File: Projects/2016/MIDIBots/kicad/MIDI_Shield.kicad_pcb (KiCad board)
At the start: 2 copper layers, 92.7 x 82.5 mm, 71 parts, among them IC1 PC900V, K1 SRVO1, K2 SRVO2, K3 SRVO3, P10 A3, P11 A4, P12 AUX_12V, P13 AUX_12V, P14 AUX_5V, P15 AUX_5V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

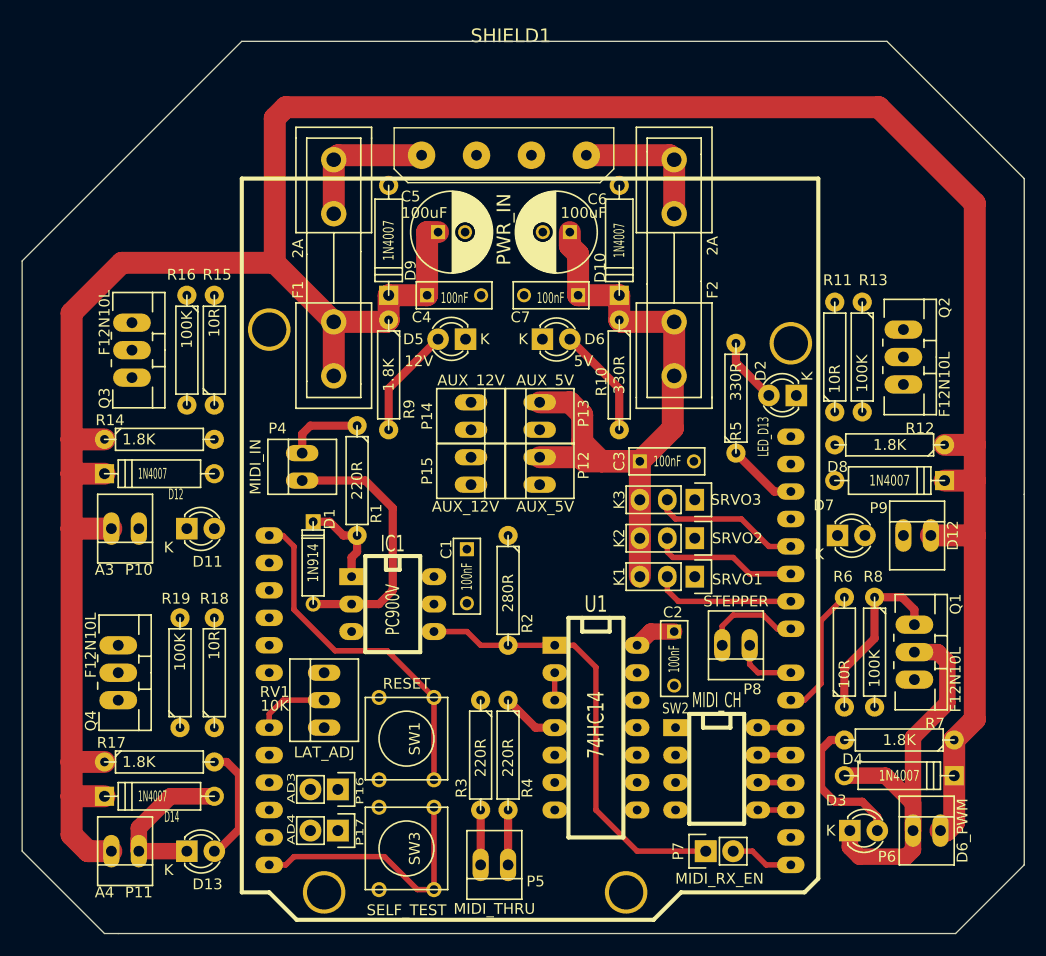
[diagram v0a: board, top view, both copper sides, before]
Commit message: [Y] Flip resistors around MOSFET circuits and reroute tracks [Y] Add 12V aux track [Y] Route VCC tracks/zones [Y] Fixed some unconnected track segments [Y] Moved some reference labels
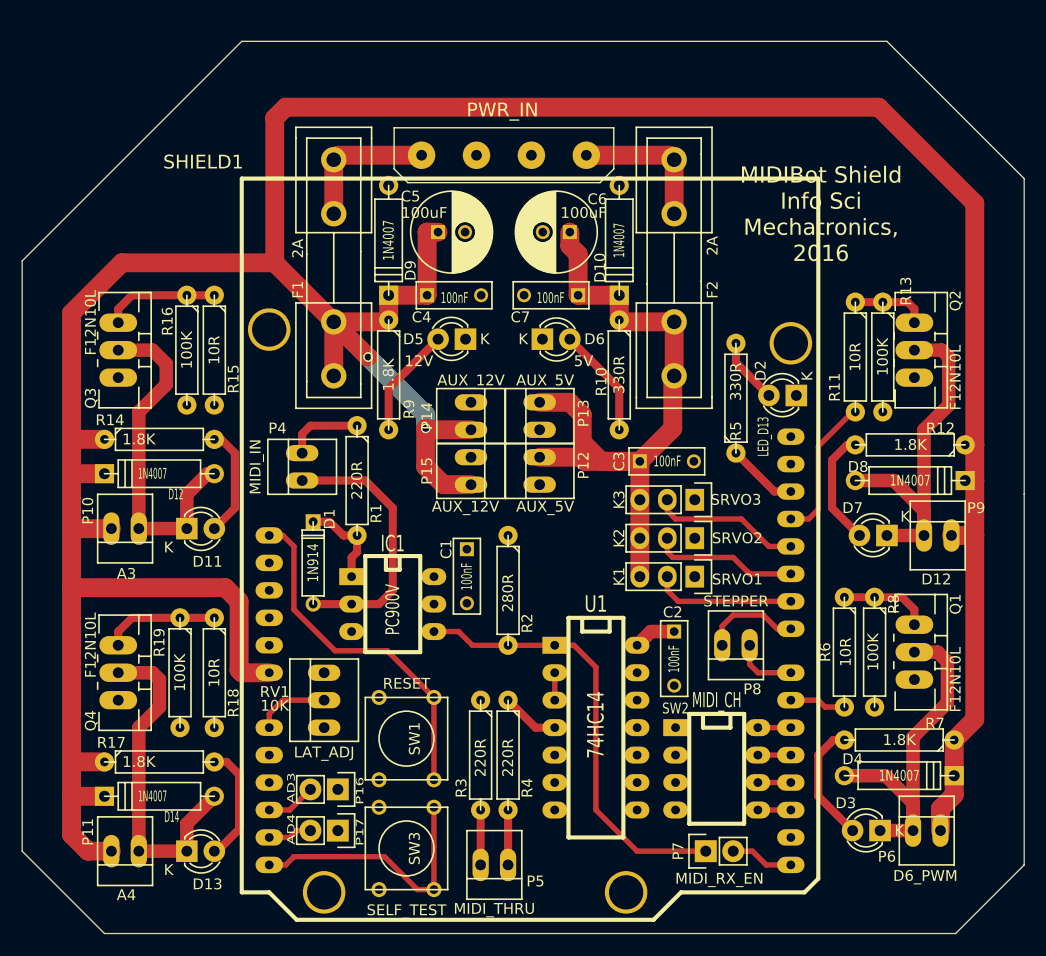
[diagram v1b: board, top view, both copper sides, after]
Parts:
- moved D7 4.57 mm to (130.8, 114.3), turned to 180 degrees
- moved D3 2.79 mm to (130.2, 141.6), turned to 180 degrees
- moved D8 1.91 mm to (133.0, 109.2)
- moved R11 1.91 mm to (127.9, 97.8), turned to 270 degrees
- moved R12 1.91 mm to (133.0, 105.9)
- moved R13 1.91 mm to (130.4, 97.8)
- moved P9 1.90 mm to (135.5, 114.3)
- moved Q3 1.27 mm to (59.7, 97.2)
- moved Q2 1.20 mm to (133.3, 97.2)
- turned R15 to 270 degrees
- turned R18 to 270 degrees
- turned R19 to 270 degrees
- turned R6 to 270 degrees
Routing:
- net +12V: track 271.3 -> 316.6 mm, vias 0 -> 2
- net Net-(D7-Pad1): track 0.00 -> 34.1 mm
- net Net-(D11-Pad1): track 0.00 -> 32.2 mm
- net Net-(D13-Pad1): track 15.9 -> 32.5 mm
- net /MOSFET_2: track 0.00 -> 13.5 mm
- net Net-(D7-Pad2): track 0.00 -> 10.8 mm
- net Net-(Q4-Pad1): track 0.00 -> 10.7 mm
- net Net-(Q3-Pad1): track 0.00 -> 10.7 mm
- net Net-(D11-Pad2): track 0.00 -> 10.2 mm
- net Net-(Q1-Pad1): track 16.9 -> 8.35 mm
- net /MOSFET_1_PWM: track 12.3 -> 5.22 mm
- net Net-(Q2-Pad1): track 0.00 -> 6.99 mm
- net Net-(D3-Pad1): track 40.1 -> 33.3 mm
- net /AD3: track 0.00 -> 4.60 mm
- net /AD4: track 0.00 -> 4.07 mm
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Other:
- net class Current_Loop: trace_width 0.762 -> 0.75
- net class Default: trace_width 0.254 -> 0.3
- net class Logic: trace_width 0.508 -> 0.5
- net class Power: trace_width 1.524 -> 1.25
- net class Power_Distribution: trace_width 2.032 -> 1.75
- board text added: "MIDIBot Shield Info Sci Mechatronics, 2016"

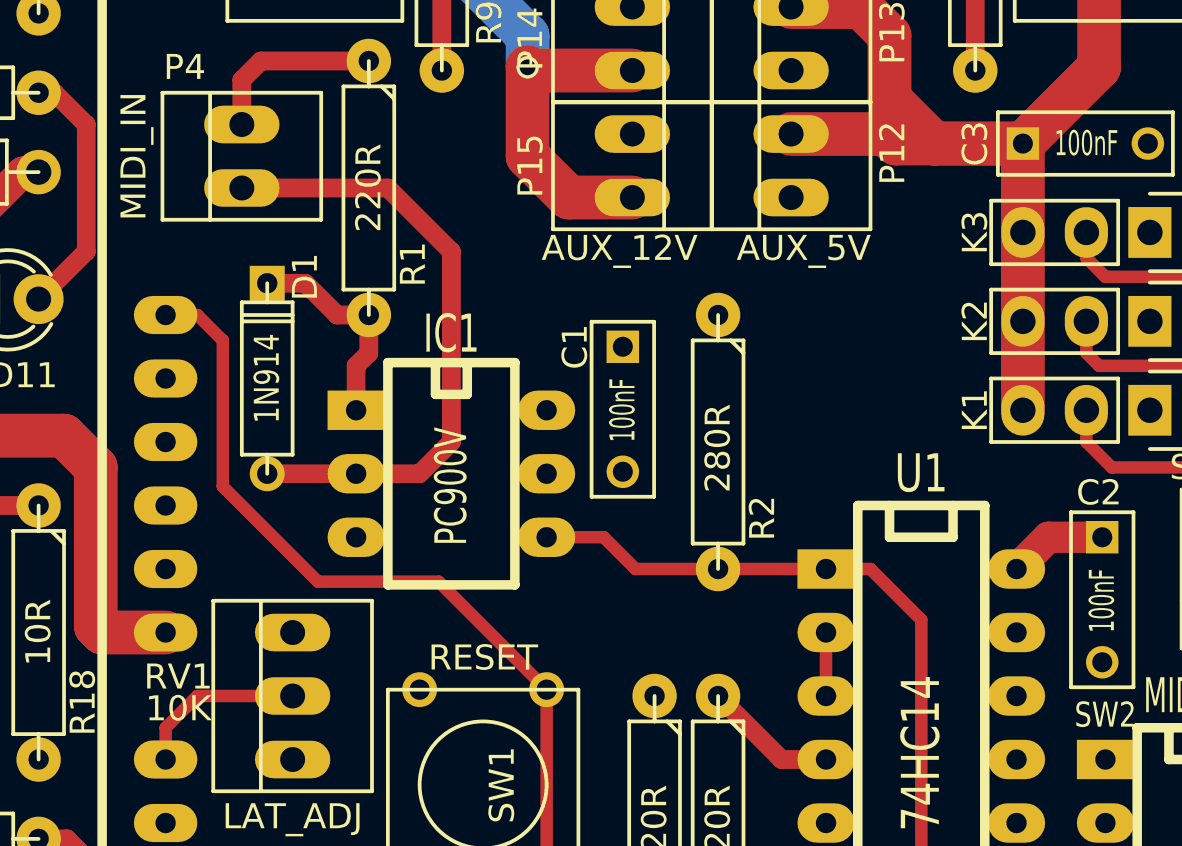
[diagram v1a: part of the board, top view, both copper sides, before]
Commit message: Routed Vcc (logic +5V) supply
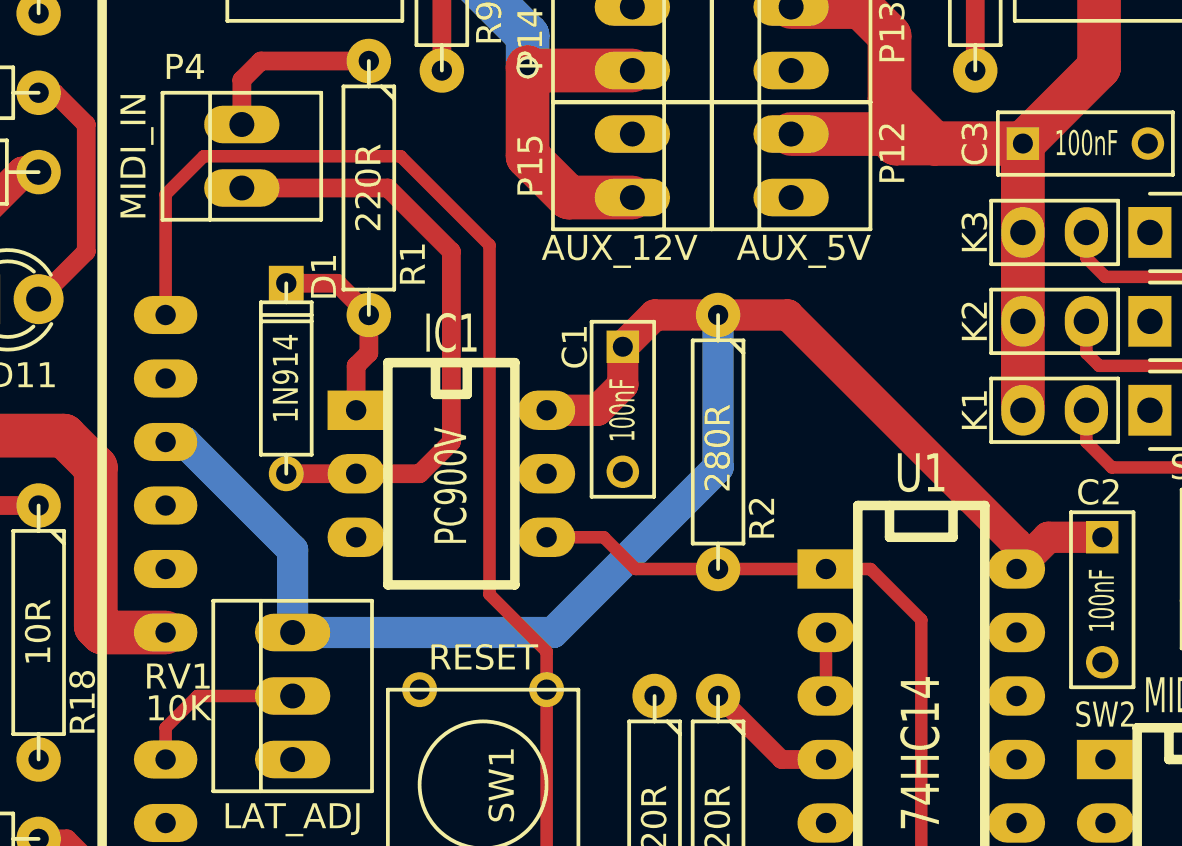
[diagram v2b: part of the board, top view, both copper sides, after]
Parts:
- moved D1 0.76 mm to (78.5, 116.8)
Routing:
- net VCC: track 3.96 -> 66.0 mm
- net /RESET: track 32.5 -> 46.2 mm
- net Net-(D1-Pad2): track 24.9 -> 24.2 mm
- net Net-(D1-Pad1): track 8.61 -> 7.85 mm
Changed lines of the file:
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@@
   (general
     (links 151)
-    (no_connects 56)
+    (no_connects 51)
     (area 50.749999 68.529999 143.560001 151.180001)
     (thickness 1.6)
     (drawings 19)
-    (tracks 249)
+    (tracks 263)
     (zones 0)
     (modules 71)
@@
   )
   (module Discret:D3 (layer F.Cu)
-    (at 77.724 116.84 90)
+    (at 78.486 116.84 90)
     (descr "Diode 3 pas")
     (tags "DIODE DEV")
@@
   (segment (start 118.872 134.62) (end 121.92 134.62) (width 0.5) (layer F.Cu) (net 3))
   (segment (start 118.872 132.08) (end 121.92 132.08) (width 0.5) (layer F.Cu) (net 4))
-  (segment (start 95.758 124.46) (end 92.456 124.46) (width 0.5) (layer F.Cu) (net 5) (status 400000))
-  (segment (start 91.186 123.19) (end 88.9 123.19) (width 0.5) (layer F.Cu) (net 5) (status 800000))
+  (segment (start 95.758 124.46) (end 92.456 124.46) (width 0.5) (layer F.Cu) (net 5))
+  (segment (start 91.186 123.19) (end 88.9 123.19) (width 0.5) (layer F.Cu) (net 5))
   (segment (start 92.456 124.46) (end 91.186 123.19) (width 0.5) (layer F.Cu) (net 5))
-  (segment (start 100.076 124.46) (end 95.758 124.46) (width 0.5) (layer F.Cu) (net 5) (status C00000))
+  (segment (start 100.076 124.46) (end 95.758 124.46) (width 0.5) (layer F.Cu) (net 5))
   (segment (start 100.076 124.46) (end 101.854 124.46) (width 0.5) (layer F.Cu) (net 5))
   (segment (start 107.696 143.51) (end 114.046 143.51) (width 0.5) (layer F.Cu) (net 5))
@@
   (segment (start 103.886 126.492) (end 103.886 139.7) (width 0.5) (layer F.Cu) (net 5))
   (segment (start 101.854 124.46) (end 103.886 126.492) (width 0.5) (layer F.Cu) (net 5))
-  (segment (start 73.66 114.3) (end 74.93 114.3) (width 0.5) (layer F.Cu) (net 6))
-  (segment (start 74.93 114.3) (end 75.946 115.316) (width 0.5) (layer F.Cu) (net 6))
-  (segment (start 75.946 115.316) (end 75.946 121.158) (width 0.5) (layer F.Cu) (net 6))
-  (segment (start 75.946 121.158) (end 79.756 124.968) (width 0.5) (layer F.Cu) (net 6))
-  (segment (start 79.756 124.968) (end 84.582 124.968) (width 0.5) (layer F.Cu) (net 6))
-  (segment (start 84.582 124.968) (end 88.9 129.286) (width 0.5) (layer F.Cu) (net 6))
+  (segment (start 88.9 129.286) (end 88.9 127.762) (width 0.5) (layer F.Cu) (net 6))
+  (segment (start 73.66 109.474) (end 73.66 114.3) (width 0.5) (layer F.Cu) (net 6))
+  (segment (start 75.184 107.95) (end 73.66 109.474) (width 0.5) (layer F.Cu) (net 6))
+  (segment (start 83.058 107.95) (end 75.184 107.95) (width 0.5) (layer F.Cu) (net 6))
+  (segment (start 86.614 111.506) (end 83.058 107.95) (width 0.5) (layer F.Cu) (net 6))
+  (segment (start 86.614 125.476) (end 86.614 111.506) (width 0.5) (layer F.Cu) (net 6))
+  (segment (start 88.9 127.762) (end 86.614 125.476) (width 0.5) (layer F.Cu) (net 6))
   (segment (start 88.9 129.286) (end 88.9 136.906) (width 0.5) (layer F.Cu) (net 6))
   (segment (start 107.95 110.998) (end 107.95 114.554) (width 1.75) (layer F.Cu) (net 8))
@@
   (segment (start 110.49 112.014) (end 110.49 110.998) (width 0.5) (layer F.Cu) (net 21))
   (segment (start 100.076 127) (end 100.076 129.54) (width 0.5) (layer F.Cu) (net 22))
+  (segment (start 78.74 127) (end 89.154 127) (width 1.25) (layer B.Cu) (net 23) (status 400000))
+  (segment (start 95.758 120.396) (end 95.758 114.3) (width 1.25) (layer B.Cu) (net 23) (status 800000))
+  (segment (start 89.154 127) (end 95.758 120.396) (width 1.25) (layer B.Cu) (net 23))
+  (segment (start 73.66 119.38) (end 74.422 119.38) (width 1.25) (layer B.Cu) (net 23) (status C00000))
+  (segment (start 74.422 119.38) (end 78.74 123.698) (width 1.25) (layer B.Cu) (net 23) (status 400000))
+  (segment (start 78.74 123.698) (end 78.74 127) (width 1.25) (layer B.Cu) (net 23) (status 800000))
+  (segment (start 91.948 115.57) (end 91.948 117.094) (width 1.25) (layer F.Cu) (net 23))
+  (segment (start 90.932 118.11) (end 88.9 118.11) (width 1.25) (layer F.Cu) (net 23))
+  (segment (start 91.948 117.094) (end 90.932 118.11) (width 1.25) (layer F.Cu) (net 23))
+  (segment (start 95.758 114.3) (end 93.218 114.3) (width 1.25) (layer F.Cu) (net 23))
+  (segment (start 93.218 114.3) (end 91.948 115.57) (width 1.25) (layer F.Cu) (net 23))
+  (segment (start 107.696 124.46) (end 107.696 123.444) (width 1.25) (layer F.Cu) (net 23))
+  (segment (start 107.696 123.444) (end 98.552 114.3) (width 1.25) (layer F.Cu) (net 23))
+  (segment (start 98.552 114.3) (end 95.758 114.3) (width 1.25) (layer F.Cu) (net 23))
   (segment (start 111.125 123.19) (end 108.966 123.19) (width 1.25) (layer F.Cu) (net 23))
   (segment (start 108.966 123.19) (end 107.696 124.46) (width 1.25) (layer F.Cu) (net 23))
@@
   (segment (start 136.398 125.984) (end 136.398 129.794) (width 1.25) (layer F.Cu) (net 24))
   (segment (start 135.509 125.095) (end 136.398 125.984) (width 1.25) (layer F.Cu) (net 24))
-  (segment (start 92.329 109.601) (end 89.789 109.601) (width 1.75) (layer F.Cu) (net 25) (status 400000))
+  (segment (start 92.329 109.601) (end 89.789 109.601) (width 1.75) (layer F.Cu) (net 25))
   (segment (start 88.138 107.95) (end 88.138 104.394) (width 1.75) (layer F.Cu) (net 25))
   (segment (start 89.789 109.601) (end 88.138 107.95) (width 1.75) (layer F.Cu) (net 25))
-  (segment (start 79.629 94.53626) (end 79.629 94.615) (width 1.75) (layer F.Cu) (net 25) (status C00000))
-  (segment (start 79.629 94.615) (end 82.804 97.79) (width 1.75) (layer F.Cu) (net 25) (status 400000))
-  (segment (start 88.265 104.521) (end 92.329 104.521) (width 1.75) (layer F.Cu) (net 25) (status 800000))
+  (segment (start 79.629 94.53626) (end 79.629 94.615) (width 1.75) (layer F.Cu) (net 25))
+  (segment (start 79.629 94.615) (end 82.804 97.79) (width 1.75) (layer F.Cu) (net 25))
+  (segment (start 88.265 104.521) (end 92.329 104.521) (width 1.75) (layer F.Cu) (net 25))
   (segment (start 88.138 104.394) (end 88.265 104.521) (width 1.75) (layer F.Cu) (net 25))
   (via (at 88.138 104.394) (size 0.889) (drill 0.635) (layers F.Cu B.Cu) (net 25))
@@
   (segment (start 82.804 97.79) (end 88.138 103.124) (width 1.75) (layer B.Cu) (net 25))
   (via (at 82.804 97.79) (size 0.889) (drill 0.635) (layers F.Cu B.Cu) (net 25))
-  (segment (start 135.763 141.605) (end 135.763 139.573) (width 1.75) (layer F.Cu) (net 25) (status 400000))
-  (segment (start 137.033 138.303) (end 137.033 136.525) (width 1.75) (layer F.Cu) (net 25) (status 800000))
+  (segment (start 135.763 141.605) (end 135.763 139.573) (width 1.75) (layer F.Cu) (net 25))
+  (segment (start 137.033 138.303) (end 137.033 136.525) (width 1.75) (layer F.Cu) (net 25))
   (segment (start 135.763 139.573) (end 137.033 138.303) (width 1.75) (layer F.Cu) (net 25))
-  (segment (start 137.033 133.223) (end 137.033 136.525) (width 1.75) (layer F.Cu) (net 25) (status C00000))
+  (segment (start 137.033 133.223) (end 137.033 136.525) (width 1.75) (layer F.Cu) (net 25))
   (segment (start 73.66 127) (end 71.12 127) (width 1.75) (layer F.Cu) (net 25))
   (segment (start 69.596 119.126) (end 55.372 119.126) (width 1.75) (layer F.Cu) (net 25))
@@
   (segment (start 110.71098 79.121) (end 111.125 79.53502) (width 1.75) (layer F.Cu) (net 32))
   (segment (start 111.125 79.53502) (end 111.125 84.53374) (width 1.75) (layer F.Cu) (net 32))
+  (segment (start 78.486 113.03) (end 80.518 113.03) (width 0.75) (layer F.Cu) (net 33) (status 400000))
+  (segment (start 80.518 113.03) (end 81.788 114.3) (width 0.75) (layer F.Cu) (net 33) (status 800000))
   (segment (start 81.788 114.3) (end 81.788 115.824) (width 0.75) (layer F.Cu) (net 33))
   (segment (start 81.28 116.332) (end 81.28 118.11) (width 0.75) (layer F.Cu) (net 33))
   (segment (start 81.788 115.824) (end 81.28 116.332) (width 0.75) (layer F.Cu) (net 33))
-  (segment (start 81.788 114.3) (end 80.518 114.3) (width 0.75) (layer F.Cu) (net 33))
-  (segment (start 79.248 113.03) (end 77.724 113.03) (width 0.75) (layer F.Cu) (net 33))
-  (segment (start 80.518 114.3) (end 79.248 113.03) (width 0.75) (layer F.Cu) (net 33))
+  (segment (start 78.486 120.65) (end 81.28 120.65) (width 0.75) (layer F.Cu) (net 34) (status C00000))
   (segment (start 76.708 109.22) (end 82.55 109.22) (width 0.75) (layer F.Cu) (net 34))
   (segment (start 83.82 120.65) (end 81.28 120.65) (width 0.75) (layer F.Cu) (net 34))
@@
   (segment (start 85.09 111.76) (end 85.09 119.38) (width 0.75) (layer F.Cu) (net 34))
   (segment (start 82.55 109.22) (end 85.09 111.76) (width 0.75) (layer F.Cu) (net 34))
-  (segment (start 77.724 120.65) (end 81.28 120.65) (width 0.75) (layer F.Cu) (net 34))
   (segment (start 116.84 96.52) (end 116.84 98.298) (width 0.75) (layer F.Cu) (net 35))
   (segment (start 116.84 98.298) (end 119.888 101.346) (width 0.75) (layer F.Cu) (net 35))

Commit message: Re-re-routed RESET track
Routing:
- net /RESET: track 46.2 -> 32.6 mm
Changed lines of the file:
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@@
     (thickness 1.6)
     (drawings 19)
-    (tracks 263)
+    (tracks 262)
     (zones 0)
     (modules 71)
@@
   (segment (start 103.886 126.492) (end 103.886 139.7) (width 0.5) (layer F.Cu) (net 5))
   (segment (start 101.854 124.46) (end 103.886 126.492) (width 0.5) (layer F.Cu) (net 5))
-  (segment (start 88.9 129.286) (end 88.9 127.762) (width 0.5) (layer F.Cu) (net 6))
-  (segment (start 73.66 109.474) (end 73.66 114.3) (width 0.5) (layer F.Cu) (net 6))
-  (segment (start 75.184 107.95) (end 73.66 109.474) (width 0.5) (layer F.Cu) (net 6))
-  (segment (start 83.058 107.95) (end 75.184 107.95) (width 0.5) (layer F.Cu) (net 6))
-  (segment (start 86.614 111.506) (end 83.058 107.95) (width 0.5) (layer F.Cu) (net 6))
-  (segment (start 86.614 125.476) (end 86.614 111.506) (width 0.5) (layer F.Cu) (net 6))
-  (segment (start 88.9 127.762) (end 86.614 125.476) (width 0.5) (layer F.Cu) (net 6))
+  (segment (start 73.66 114.3) (end 75.692 114.3) (width 0.5) (layer F.Cu) (net 6) (status 400000))
+  (segment (start 86.614 127) (end 88.9 129.286) (width 0.5) (layer F.Cu) (net 6) (status 800000))
+  (segment (start 82.296 127) (end 86.614 127) (width 0.5) (layer F.Cu) (net 6))
+  (segment (start 76.708 121.412) (end 82.296 127) (width 0.5) (layer F.Cu) (net 6))
+  (segment (start 76.708 115.316) (end 76.708 121.412) (width 0.5) (layer F.Cu) (net 6))
+  (segment (start 75.692 114.3) (end 76.708 115.316) (width 0.5) (layer F.Cu) (net 6))
   (segment (start 88.9 129.286) (end 88.9 136.906) (width 0.5) (layer F.Cu) (net 6))
   (segment (start 107.95 110.998) (end 107.95 114.554) (width 1.75) (layer F.Cu) (net 8))
